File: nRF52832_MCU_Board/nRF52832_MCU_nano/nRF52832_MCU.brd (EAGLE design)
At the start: 45.7 x 22.9 mm, 19 parts, among them J1 TSW-116-02-S-S, J2 TSW-116-02-S-S, U1 NRF52832, X1 32MHz

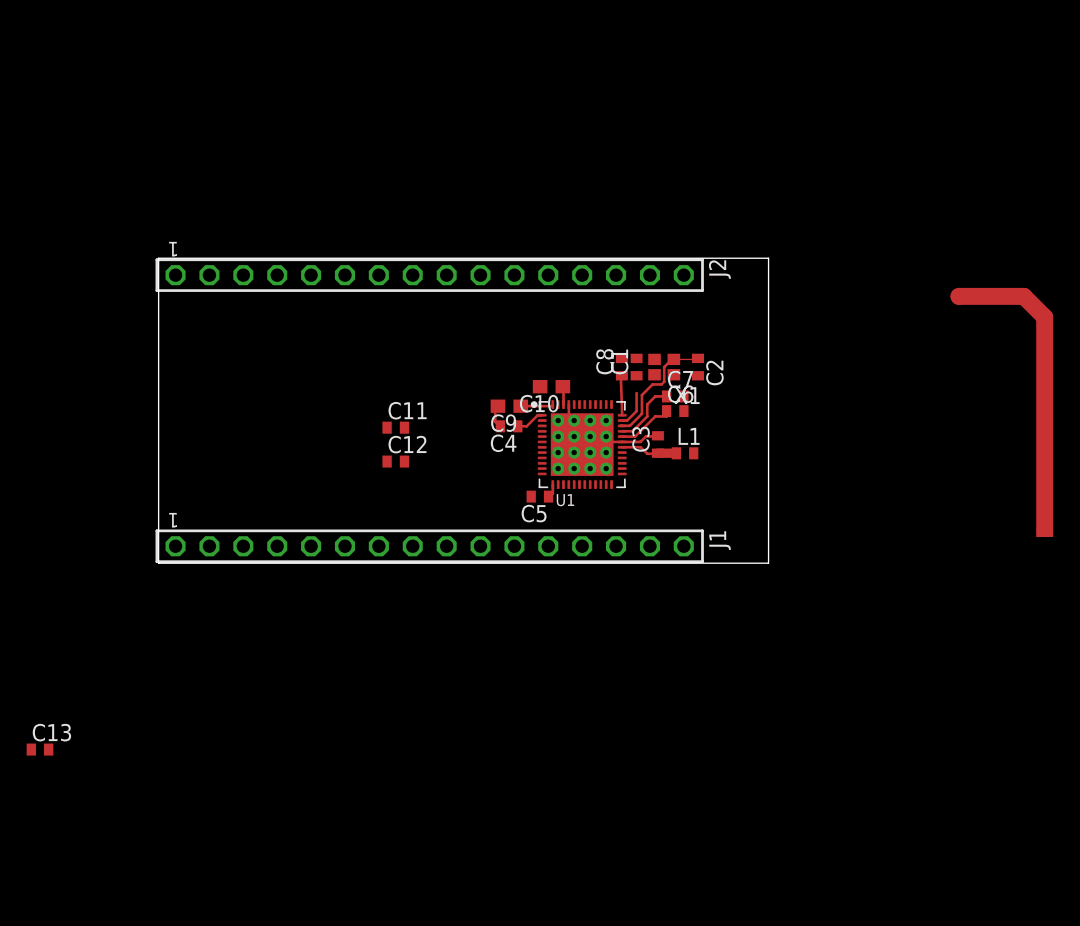
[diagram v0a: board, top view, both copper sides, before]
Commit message: Routed gpio
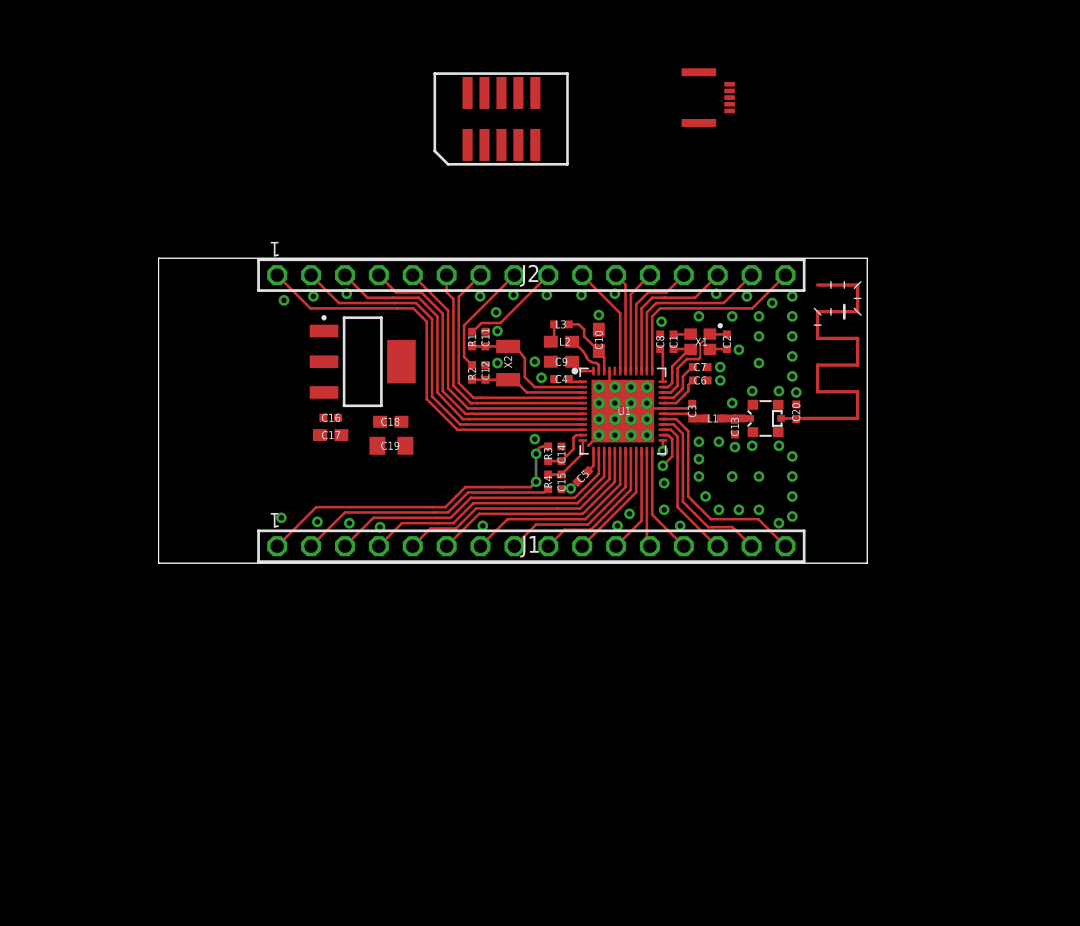
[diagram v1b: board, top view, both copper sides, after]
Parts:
- added C14, C15: 300pF, nRF:RESC0402_N
- added C16: 100nF, nRF:RESC0402_N
- added C17, C18: 10µF, nRF:RESC0603_N
- added C19: 100µF, nRF:RESC0805_N
- added C20: (no value), nRF:RESC0402_N
- added J3: MM8130-2600, nRF:MM8130-2600
- added J4: FPC_05P-RA-SMD, nRF:FPC_05P-RA-SMD
- added J5: DEBUG_CONNECTOR, nRF:HDRV127P5X2-10_N
- added L2: 10µH, nRF:RESC0603_N
- added L3: 15nH, nRF:RESC0402_N
- added R1, R2, R3, R4: 0R, nRF:RESC0402_N
- added U$2: TLV1117, nRF:SOT220P700-4_N
- added X2: 32.768kHz, nRF:XTAL_3215_N
- ANT1: value 2.45GHZ_PCB_ANTENNA -> (none); device nRF:PCB_ANTENNA -> nRF:QWMP_MEANDERED_LEFT_+6
- C1, C11, C12, C2, C3, C4, C5, C6, C7, C8: device rcl:C0402 -> nRF:RESC0402_N
- C10, C9: device rcl:C0603 -> nRF:RESC0603_N
- C13: value 0.8pF -> (none); device rcl:C0402 -> nRF:RESC0402_N
- L1: device nRF:R0402 -> nRF:RESC0402_N
- U1: device nRF:QFN40P600X600X90-48N -> nRF:QFN40P600X600X90-48_N
- X1: device nRF:BT-XTAL_2016 -> nRF:BT-XTAL_2016_N
- moved C13 57.4 mm to (43.2, 10.2), turned to 270 degrees
- moved ANT1 14.8 mm to (48.4, 10.8)
- moved C12 9.48 mm to (24.5, 14.3), turned to 270 degrees
- moved C11 9.45 mm to (24.5, 16.8), turned to 270 degrees
- moved J1 7.62 mm to (27.9, 1.27)
- moved J2 7.62 mm to (27.9, 21.6)
- moved C4 5.29 mm to (30.2, 13.8)
- moved C9 5.14 mm to (30.2, 15.1)
- moved C10 4.96 mm to (33.0, 16.7), turned to 90 degrees
- moved U1 3.95 mm to (34.8, 11.4)
- moved C3 3.59 mm to (40.0, 11.4)
- moved C5 3.56 mm to (31.8, 6.50), turned to 225 degrees
- moved C8 3.44 mm to (37.6, 16.6)
- moved L1 3.38 mm to (41.6, 10.8)
- moved C1 3.36 mm to (38.6, 16.6)
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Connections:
- removed net N$14: U1.26
- removed net N$15: U1.25
- removed net P0.18: J2.14, U1.21
- removed net P0.21: J2.11, U1.24
- removed net VCC: C5.1, C8.1, C9.1, U1.13, U1.36, U1.48
- new net N$2: L2.2, L3.1
- new net N$5: C13.1, J3.IN, L1.2
- new net NFC1: C14.2, J4.2, R3.1, U1.11
- new net NFC2: C15.1, J4.4, R4.2, U1.12
- new net P0.18/SWO: J1.10, J5.10, U1.21
- new net P0.21/RESET: J1.13, J5.6, U1.24
- new net SWDCLK: J5.4, U1.25
- new net SWDIO: J5.2, U1.26
- new net VCC_P3V3: C18.1, C19.1, C5.1, C8.1, C9.1, J5.1, U$2.2, U$2.4, U1.13, U1.36, U1.48
- new net VCC_P5V0: C16.1, C17.1, U$2.3
- new net X1: C2.1, U1.34, X1.1
- new net XL1: C11.2, R1.1, U1.2, X2.1
- new net XL2: C12.2, R2.2, U1.3, X2.2
- net DEC4: now also L3.2
- net GND: now also C11.1, C12.1, C14.1, C15.2, C16.2, C17.2, C18.2, C19.2, C20.2, J3.1, J3.2, J3.3, J3.4, J5.3, J5.5, J5.9, U$2.1, X1.2, X1.4; no longer X1.P$2, X1.P$4
- net N$1: now also C20.1, J3.OUT; no longer C13.1, L1.2
- net N$3: now also X1.3; no longer X1.P$3
- net N$4: now also L2.1, U1.47; no longer C2.1, U1.34, X1.P$1
- net P0.00: now also J2.9, R1.2; no longer J1.1, U1.2
- net P0.01: now also J2.8, R2.1; no longer J1.2, U1.3
- net P0.02: now also J2.7; no longer J1.3
- net P0.03: now also J2.6; no longer J1.4
- net P0.04: now also J2.5; no longer J1.5
- net P0.05: now also J2.4; no longer J1.6
- net P0.06: now also J2.3; no longer J1.7
- net P0.07: now also J2.2; no longer J1.8
- net P0.08: now also J2.1; no longer J1.9
- net P0.09: now also J1.1, R3.2; no longer J1.10, U1.11
- net P0.10: now also J1.2, R4.1; no longer J1.11, U1.12
- net P0.11: now also J1.3; no longer J1.12
- net P0.12: now also J1.4; no longer J1.13
- net P0.13: now also J1.5; no longer J1.14
- net P0.14: now also J1.6; no longer J1.15
- net P0.15: now also J1.7; no longer J1.16
- net P0.16: now also J1.8; no longer J2.16
- net P0.17: now also J1.9; no longer J2.15
- net P0.19: now also J1.11; no longer J2.13
- net P0.20: now also J1.12; no longer J2.12
- net P0.22: now also J1.14; no longer J2.10
- net P0.23: now also J1.15; no longer J2.9
- net P0.24: now also J1.16; no longer J2.8
- net P0.25: now also J2.16; no longer J2.7
- net P0.26: now also J2.15; no longer J2.6
- net P0.27: now also J2.14; no longer J2.5
- net P0.28: now also J2.13; no longer J2.4
- net P0.29: now also J2.12; no longer J2.3
- net P0.30: now also J2.11; no longer J2.2
- net P0.31: now also J2.10; no longer J2.1
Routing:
- net P0.08: track 0.00 -> 31.1 mm
- net P0.07: track 0.00 -> 28.4 mm
- net P0.06: track 0.00 -> 25.7 mm
- net P0.09: track 0.00 -> 24.6 mm, vias 0 -> 2
- net P0.05: track 0.00 -> 23.0 mm
- net P0.11: track 0.00 -> 23.0 mm
- net P0.12: track 0.00 -> 21.0 mm
- net P0.04: track 0.00 -> 20.3 mm
- net P0.10: track 0.00 -> 19.5 mm
- net P0.13: track 0.00 -> 18.9 mm
- net P0.03: track 0.00 -> 18.7 mm
- net P0.02: track 0.00 -> 18.5 mm
- net P0.14: track 0.00 -> 16.9 mm
- net P0.24: track 0.00 -> 16.0 mm
- net P0.25: track 0.00 -> 15.4 mm
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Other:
- board size 45.7 x 22.9 mm -> 53.1 x 22.9 mm

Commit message: Positioned buttons, positioned powersupply
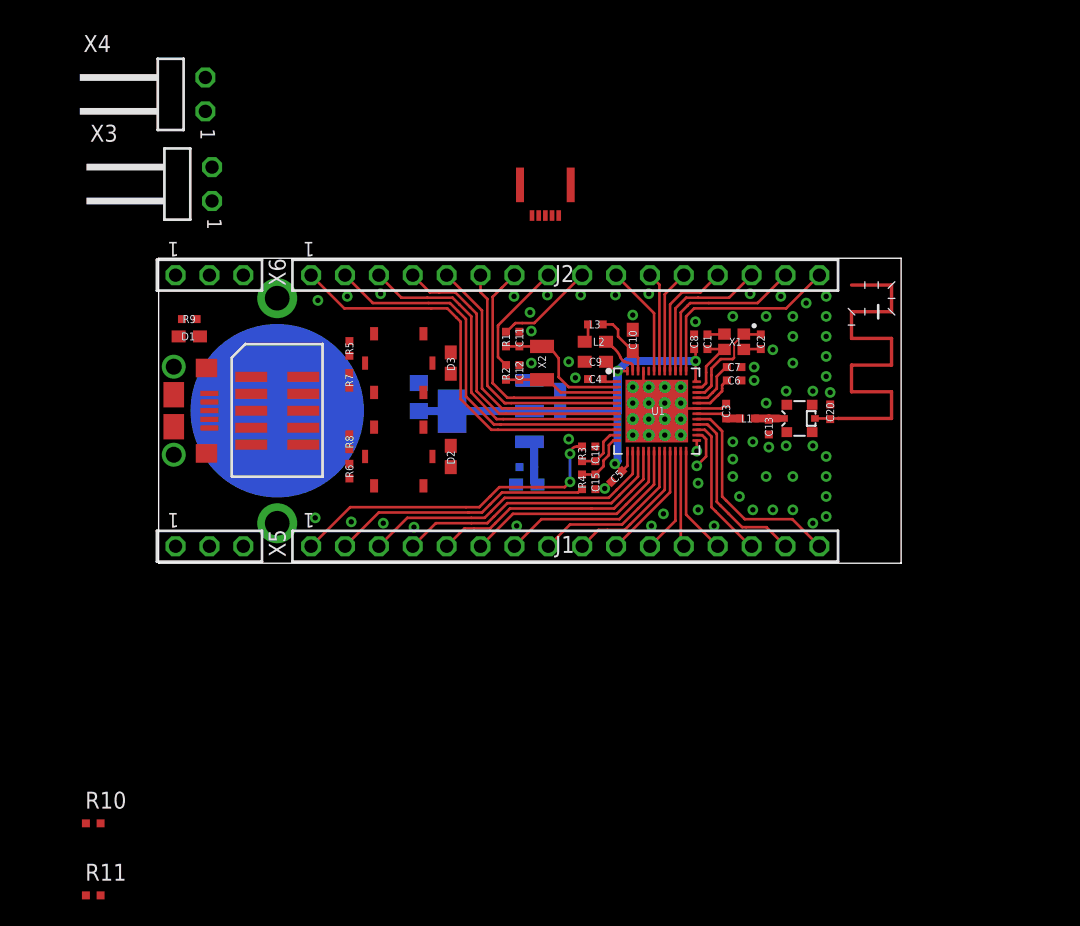
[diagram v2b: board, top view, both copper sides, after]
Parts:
- added D1, D2, D3: LED, nRF:RESC0603_N
- added R10, R11, R5, R6, R9: 330R, nRF:RESC0402_N
- added R7, R8: 100k, nRF:RESC0402_N
- added U$1: MICROUSB, nRF:USB-MICRO-B-RA-SMD-PIP
- added U$3: CR1632, nRF:CR1632_HOLDER_TH
- added U$4, U$5: PANASONIC_EVQPT5A15, nRF:PANASONIC_EVQPT5A15
- added X3, X4: TSW-102-02-S-S-RA, con-samtec:TSW-102-02-S-S-RA
- added X5, X6: TSW-103-02-S-S, con-samtec:TSW-103-02-S-S
- moved J5 27.6 mm to (8.89, 11.4), turned to 270 degrees
- moved C16 15.2 mm to (27.6, 7.20), flipped to the bottom
- moved C17 15.2 mm to (27.6, 5.90), flipped to the bottom
- moved J4 14.2 mm to (29.0, 27.7), turned to 180 degrees
- moved C18 12.8 mm to (30.1, 12.2), flipped to the bottom, turned to 90 degrees
- moved U$2 10.3 mm to (24.9, 11.4), flipped to the bottom
- moved C19 4.25 mm to (19.5, 12.5), flipped to the bottom, turned to 90 degrees
- moved C20 2.54 mm to (50.3, 11.3)
- moved U1 2.54 mm to (37.3, 11.4)
- moved C14 2.54 mm to (32.7, 8.20)
- moved C15 2.54 mm to (32.7, 6.10)
- moved C4 2.54 mm to (32.7, 13.8)
- moved C5 2.54 mm to (34.3, 6.50)
- moved C9 2.54 mm to (32.7, 15.1)
- moved L2 2.54 mm to (32.7, 16.6)
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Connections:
- new net N$6: R6.2, R8.1, U$5.1, U$5.2
- new net N$7: R5.2, R7.1, U$4.1, U$4.2
- new net VCC: R7.2, R8.2
- new net VCC_P5V0_USB: U$1.1
- net GND: now also U$1.5, U$4.3, U$4.4, U$4.5, U$4.6, U$5.3, U$5.4, U$5.5, U$5.6, X5.3, X6.3
- net VCC_P3V3: now also X5.2, X6.2
- net VCC_P5V0: now also X5.1, X6.1
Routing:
- net VCC_P3V3: track 6.08 -> 38.2 mm, vias 0 -> 3
- net VCC_P5V0: track 0.00 -> 3.45 mm
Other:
- board size 53.1 x 22.9 mm -> 55.7 x 22.9 mm

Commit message: Fixed library links
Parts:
- ANT1: device nRF:QWMP_MEANDERED_LEFT_+6 -> Nordic_misc:QWMP_MEANDERED_LEFT_+6
- C1, C11, C12, C13, C14, C15, C16, C2, C20, C3, C4, C5, C6, C7, C8, L1, L3, R1, R10, R11, R2, R3, R4, R5, R6, R7, R8, R9: device nRF:RESC0402_N -> Nordic_misc:RESC0402_N
- C10, C17, C18, C9, D1, D2, D3, L2: device nRF:RESC0603_N -> Nordic_misc:RESC0603_N
- C19: device nRF:RESC0805_N -> Nordic_misc:RESC0805_N
- J3: device nRF:MM8130-2600 -> Nordic_misc:MM8130-2600
- J4: device nRF:FPC_05P-RA-SMD -> Nordic_misc:FPC_05P-RA-SMD
- J5: device nRF:HDRV127P5X2-10_N -> Nordic_misc:HDRV127P5X2-10_N
- U$1: device nRF:USB-MICRO-B-RA-SMD-PIP -> Nordic_misc:USB-MICRO-B-RA-SMD-PIP
- U$2: device nRF:SOT220P700-4_N -> Nordic_misc:SOT220P700-4_N
- U$3: device nRF:CR1632_HOLDER_TH -> Nordic_misc:CR1632_HOLDER_TH
- U$4, U$5: device nRF:PANASONIC_EVQPT5A15 -> Nordic_misc:PANASONIC_EVQPT5A15
- U1: device nRF:QFN40P600X600X90-48_N -> Nordic_nRF:QFN40P600X600X90-48_N
- X1: device nRF:BT-XTAL_2016_N -> Nordic_nRF:BT-XTAL_2016_N
- X2: device nRF:XTAL_3215_N -> Nordic_nRF:XTAL_3215_N

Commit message: Done some layout
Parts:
- added R12: 0R, Nordic_misc:RESC0402_N
- D1, D2, D3: device Nordic_misc:RESC0603_N -> Nordic_misc:DIOC0603_N
- moved R11 49.9 mm to (19.8, 18.5)
- moved R10 43.7 mm to (16.6, 18.5)
- moved R6 0.60 mm to (14.3, 7.50), turned to 90 degrees
- moved X3 0.58 mm to (1.98, 28.7)
- moved R8 0.50 mm to (14.3, 9.60)
- moved R5 0.40 mm to (14.3, 16.5), turned to 270 degrees
- moved R7 0.30 mm to (14.3, 13.4)
- moved D3 0.20 mm to (21.9, 14.8), turned to 270 degrees
- turned D2 to 270 degrees
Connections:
- removed net VCC: R7.2, R8.2
- removed net VCC_P3V3: C18.1, C19.1, C5.1, C8.1, C9.1, J5.1, U$2.2, U$2.4, U1.13, U1.36, U1.48, X5.2, X6.2
- removed net VCC_P5V0: C16.1, C17.1, U$2.3, X5.1, X6.1
- new net N$8: D2.1, R10.2
- new net N$9: D3.1, R11.2
- new net VDD_LED: D1.2, R9.2
- new net VDD_P3V3: C18.1, C19.1, C5.1, C8.1, C9.1, D2.2, D3.2, J5.1, R7.2, R8.2, U$2.2, U$2.4, U1.13, U1.36, U1.48, X5.2, X6.2
- new net VDD_P5V0: C16.1, C17.1, D1.1, R12.2, U$2.3, X5.1, X6.1
- net GND: now also R9.1
- net P0.06: now also R11.1
- net P0.07: now also R10.1
- net P0.08: now also R5.1
- net P0.21/RESET: now also R6.1
- net VCC_P5V0_USB: now also R12.1
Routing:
- net VDD_P3V3: track 0.00 -> 70.9 mm, vias 0 -> 4
- net SWDIO: track 3.11 -> 46.2 mm, vias 1 -> 2
- net SWDCLK: track 0.80 -> 43.4 mm, vias 1 -> 3
- net VCC_P3V3: track 38.2 -> 0.00 mm, vias 3 -> 0
- net P0.21/RESET: track 8.11 -> 45.8 mm, vias 0 -> 1
- net P0.18/SWO: track 8.81 -> 37.2 mm, vias 0 -> 1
- net N$8: track 0.00 -> 12.3 mm
- net P0.06: track 25.7 -> 30.4 mm, vias 0 -> 1
- net P0.07: track 28.4 -> 32.9 mm, vias 0 -> 1
- net N$7: track 0.00 -> 4.33 mm
- net N$9: track 0.00 -> 3.54 mm
- net VDD_P5V0: track 0.00 -> 3.45 mm
- net VCC_P5V0: track 3.45 -> 0.00 mm
- net N$6: track 0.00 -> 3.33 mm
- net P0.08: track 31.1 -> 33.2 mm
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
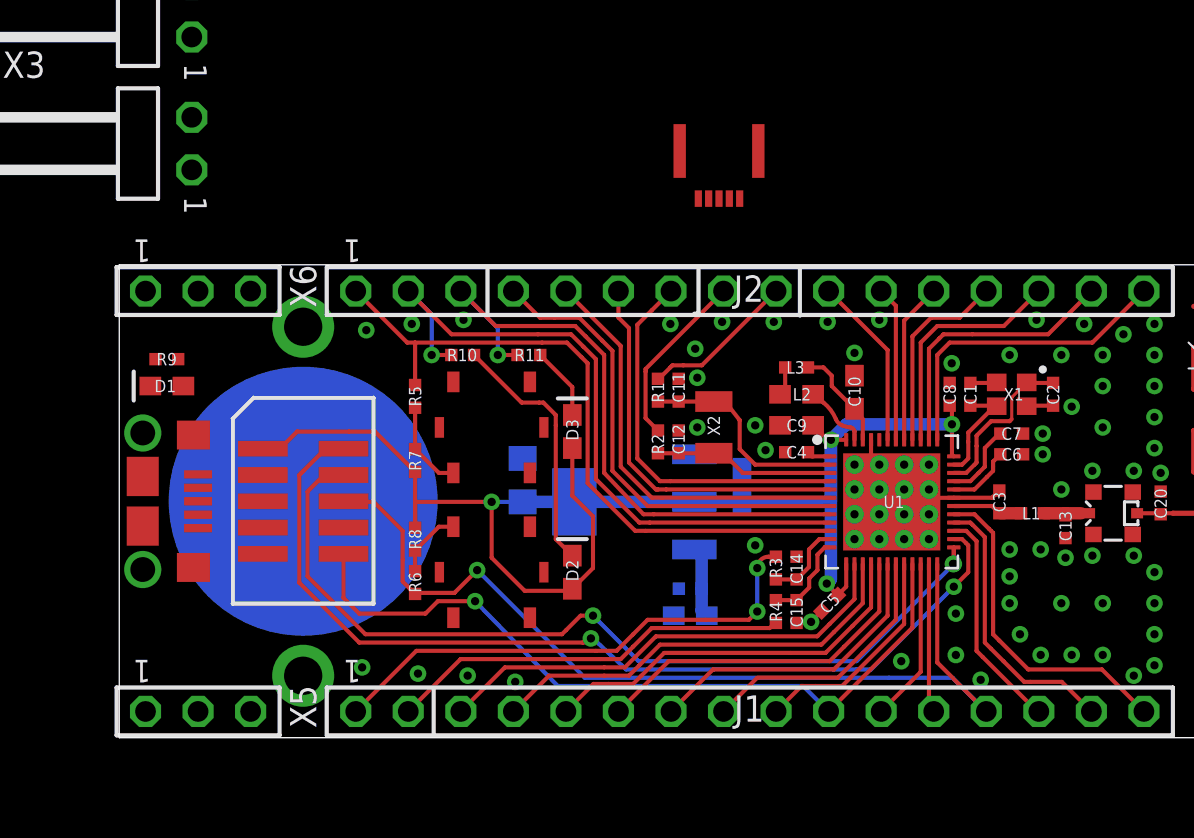
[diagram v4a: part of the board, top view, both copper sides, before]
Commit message: Squezed in nfc antenna connector
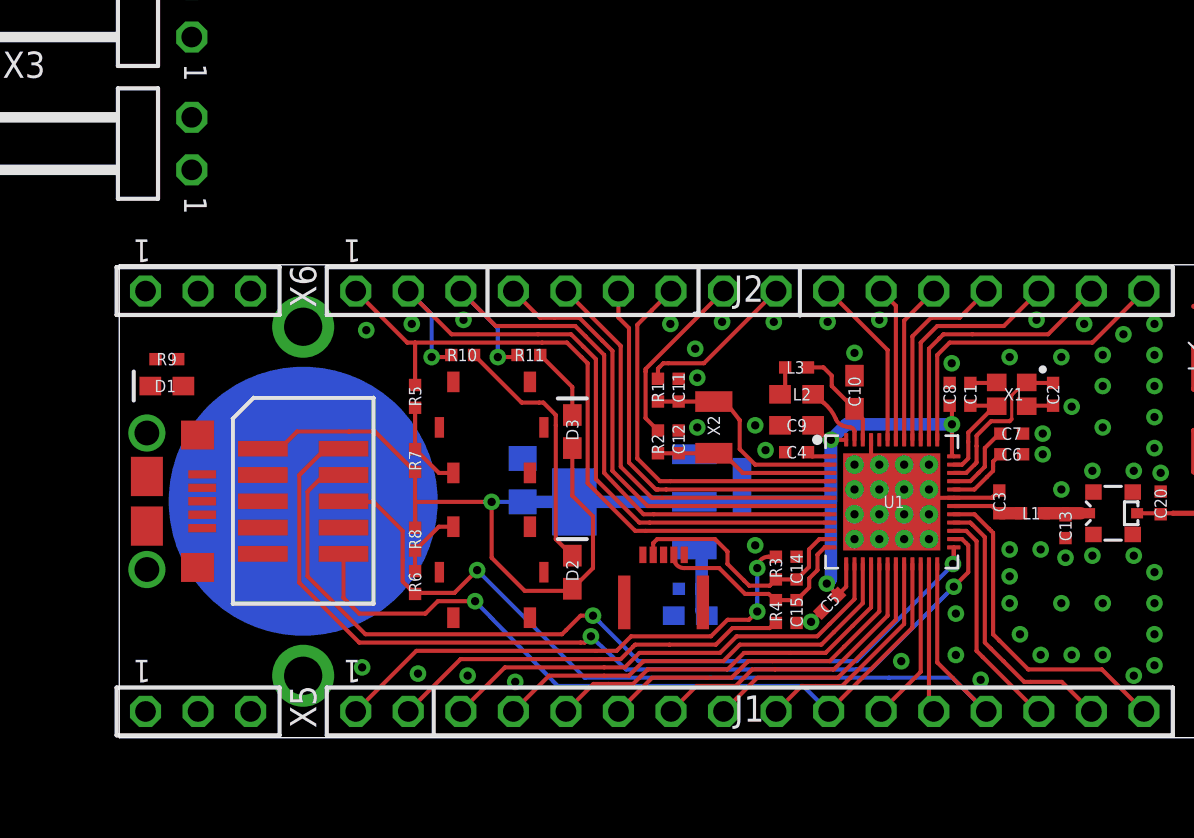
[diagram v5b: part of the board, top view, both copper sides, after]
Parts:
- moved J4 20.6 mm to (26.3, 7.24), turned to 0 degrees
- moved U$1 0.20 mm to (4.01, 11.4)
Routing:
- net NFC1: track 3.91 -> 11.9 mm
- net NFC2: track 4.35 -> 10.3 mm
- net SWDCLK: vias 3 -> 2
